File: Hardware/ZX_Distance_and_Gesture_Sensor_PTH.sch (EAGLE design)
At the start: 50 parts, among them Q1 MMBT2222A, Q2 MOSFET-NCHANNEL2N7002PW, U1 PIC16F1823-14PINTSSOP, U2 MCP6021T-E/OT, U3 DMC2700UDM, U4 DMC2700UDM, U5 BRM-2A18VERT, U6 TSOP57238TT1

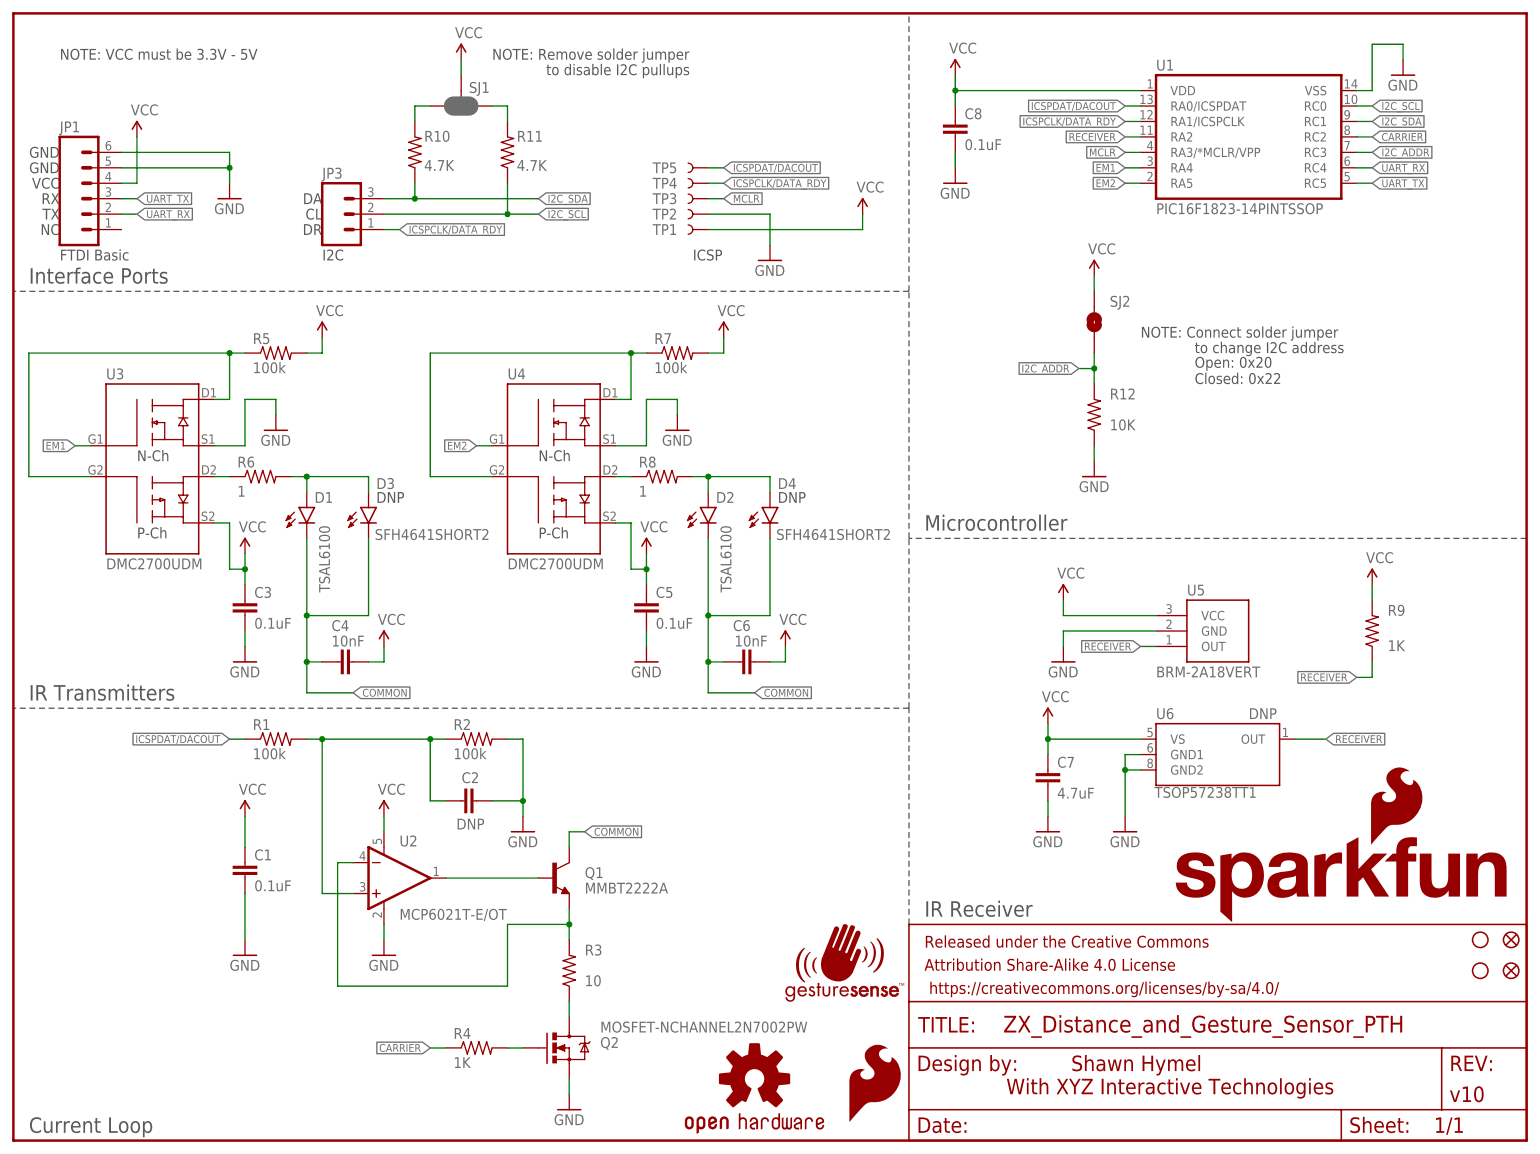
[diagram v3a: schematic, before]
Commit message: Changed to 1% 10 ohm resistor. Added Arduino I2C address to schematic.
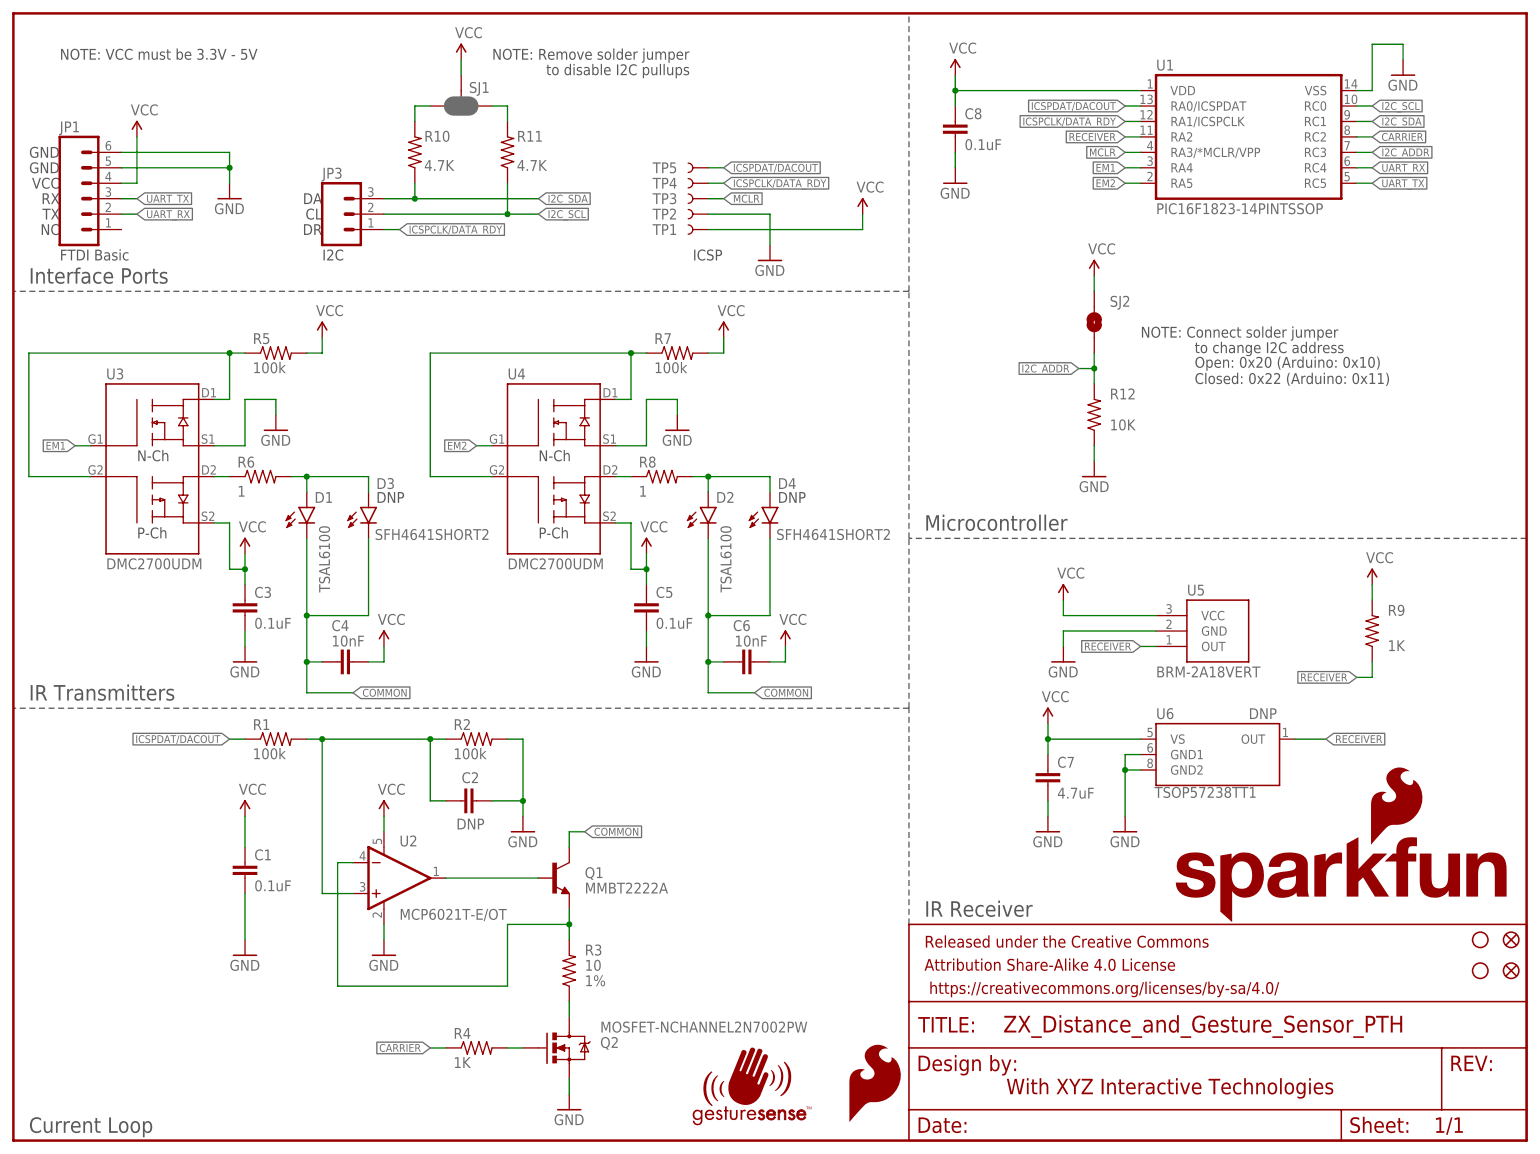
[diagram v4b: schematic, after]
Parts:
- removed LOGO2: OSHW-LOGOS, SparkFun-Aesthetics:OSHW-LOGOS
- R3: device SparkFun-Resistors:10OHM-1/10W-5%0603SMD -> SparkFun-Resistors:10OHM-1/10W-1%(0603)SMD; TOL (none) -> 1%
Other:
- note added: "Open: 0x20 (Arduino: 0x10) Closed: 0x22 (Arduino: 0x11)"
- note removed: "Open: 0x20 Closed: 0x22"
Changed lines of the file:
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@@
 <layer number="56" name="wert" color="7" fill="1" visible="no" active="no"/>
 <layer number="57" name="tCAD" color="7" fill="1" visible="no" active="no"/>
+<layer number="59" name="tCarbon" color="7" fill="1" visible="no" active="no"/>
+<layer number="60" name="bCarbon" color="7" fill="1" visible="no" active="no"/>
 <layer number="90" name="Modules" color="5" fill="1" visible="yes" active="yes"/>
 <layer number="91" name="Nets" color="2" fill="1" visible="yes" active="yes"/>
@@
 <layer number="127" name="_tValues" color="7" fill="1" visible="yes" active="yes"/>
 <layer number="128" name="_bValues" color="7" fill="1" visible="yes" active="yes"/>
+<layer number="129" name="Mask" color="7" fill="1" visible="yes" active="yes"/>
 <layer number="131" name="tAdjust" color="7" fill="1" visible="yes" active="yes"/>
 <layer number="132" name="bAdjust" color="7" fill="1" visible="yes" active="yes"/>
@@
 <layer number="223" name="223bmp" color="24" fill="1" visible="no" active="no"/>
 <layer number="224" name="224bmp" color="25" fill="1" visible="no" active="no"/>
+<layer number="225" name="225bmp" color="7" fill="1" visible="yes" active="yes"/>
+<layer number="226" name="226bmp" color="7" fill="1" visible="yes" active="yes"/>
+<layer number="227" name="227bmp" color="7" fill="1" visible="yes" active="yes"/>
+<layer number="228" name="228bmp" color="7" fill="1" visible="yes" active="yes"/>
+<layer number="229" name="229bmp" color="7" fill="1" visible="yes" active="yes"/>
+<layer number="230" name="230bmp" color="7" fill="1" visible="yes" active="yes"/>
+<layer number="231" name="231bmp" color="7" fill="1" visible="yes" active="yes"/>
 <layer number="248" name="Housing" color="7" fill="1" visible="yes" active="yes"/>
 <layer number="249" name="Edge" color="7" fill="1" visible="yes" active="yes"/>
@@
 <part name="R1" library="SparkFun-Resistors" deviceset="100KOHM-1/10W-1%(0603)" device="" value="100k"/>
 <part name="R2" library="SparkFun-Resistors" deviceset="100KOHM-1/10W-1%(0603)" device="" value="100k"/>
-<part name="R3" library="SparkFun-Resistors" deviceset="10OHM-1/10W-5%0603" device="SMD" value="10"/>
+<part name="R3" library="SparkFun-Resistors" deviceset="10OHM-1/10W-1%(0603)" device="SMD" value="10">
+<attribute name="TOL" value="1%"/>
+</part>
 <part name="R4" library="SparkFun-Resistors" deviceset="1KOHM-1/10W-1%(0603)" device="" value="1K"/>
 <part name="C1" library="SparkFun-Capacitors" deviceset="0.1UF-25V(+80/-20%)(0603)" device="" value="0.1uF"/>
@@
 <part name="U$5" library="SparkFun-Aesthetics" deviceset="SFE_LOGO_NAME_FLAME" device=".1_INCH"/>
 <part name="LOGO1" library="SparkFun-Aesthetics" deviceset="SFE_LOGO_FLAME" device=".1_INCH"/>
-<part name="LOGO2" library="SparkFun-Aesthetics" deviceset="OSHW-LOGO" device="S"/>
 <part name="STANDOFF1" library="SparkFun-Electromechanical" deviceset="STAND-OFF" device=""/>
 <part name="STANDOFF2" library="SparkFun-Electromechanical" deviceset="STAND-OFF" device=""/>
@@
 <text x="185.42" y="132.08" size="1.778" layer="97">NOTE: Connect solder jumper</text>
 <text x="194.31" y="129.54" size="1.778" layer="97">to change I2C address</text>
-<text x="194.31" y="124.46" size="1.778" layer="97">Open: 0x20
-Closed: 0x22</text>
+<text x="194.31" y="124.46" size="1.778" layer="97">Open: 0x20 (Arduino: 0x10)
+Closed: 0x22 (Arduino: 0x11)</text>
 <wire x1="147.32" y1="71.12" x2="147.32" y2="99.06" width="0.1524" layer="97" style="longdash"/>
 <wire x1="147.32" y1="99.06" x2="147.32" y2="139.7" width="0.1524" layer="97" style="longdash"/>
@@
 <instance part="R3" gate="G$1" x="91.44" y="27.94" smashed="yes" rot="R90">
 <attribute name="NAME" x="93.98" y="30.4546" size="1.778" layer="95"/>
-<attribute name="VALUE" x="93.98" y="25.4" size="1.778" layer="96"/>
+<attribute name="VALUE" x="93.98" y="27.94" size="1.778" layer="96"/>
+<attribute name="TOL" x="93.98" y="25.4" size="1.778" layer="96"/>
 </instance>
 <instance part="R4" gate="G$1" x="76.2" y="15.24"/>
@@
 <instance part="U$5" gate="G$1" x="190.5" y="35.56"/>
 <instance part="LOGO1" gate="G$1" x="137.16" y="2.54"/>
-<instance part="LOGO2" gate="G$1" x="121.92" y="10.16"/>
 <instance part="STANDOFF1" gate="G$1" x="241.3" y="33.02"/>
 <instance part="STANDOFF2" gate="G$1" x="241.3" y="27.94"/>
@@
 <instance part="SUPPLY16" gate="G$1" x="172.72" y="88.9"/>
 <instance part="GND16" gate="1" x="172.72" y="78.74"/>
-<instance part="U$6" gate="G$1" x="127" y="22.86"/>
+<instance part="U$6" gate="G$1" x="111.76" y="2.54"/>
 <instance part="D3" gate="G$1" x="58.42" y="104.14" smashed="yes">
 <attribute name="NAME" x="59.69" y="107.188" size="1.778" layer="95"/>
